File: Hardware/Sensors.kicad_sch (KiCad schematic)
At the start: 61 parts, among them J10 VL530X Connector, J11 VL530X Connector, J12 VL530X Connector, J13 VL530X Connector, J5 BNO055 Breakout, J8 VL530X Connector, J9 VL530X Connector, Q10 Q_NMOS_GSD, Q11 Q_NMOS_GSD, Q12 Q_NMOS_GSD, Q13 TEFT4300, Q2 Q_NMOS_GSD, Q3 TEFT4300, Q4 TEFT4300, Q5 TEFT4300, Q6 TEFT4300, Q7 TEFT4300, Q8 Q_NMOS_GSD, Q9 Q_NMOS_GSD

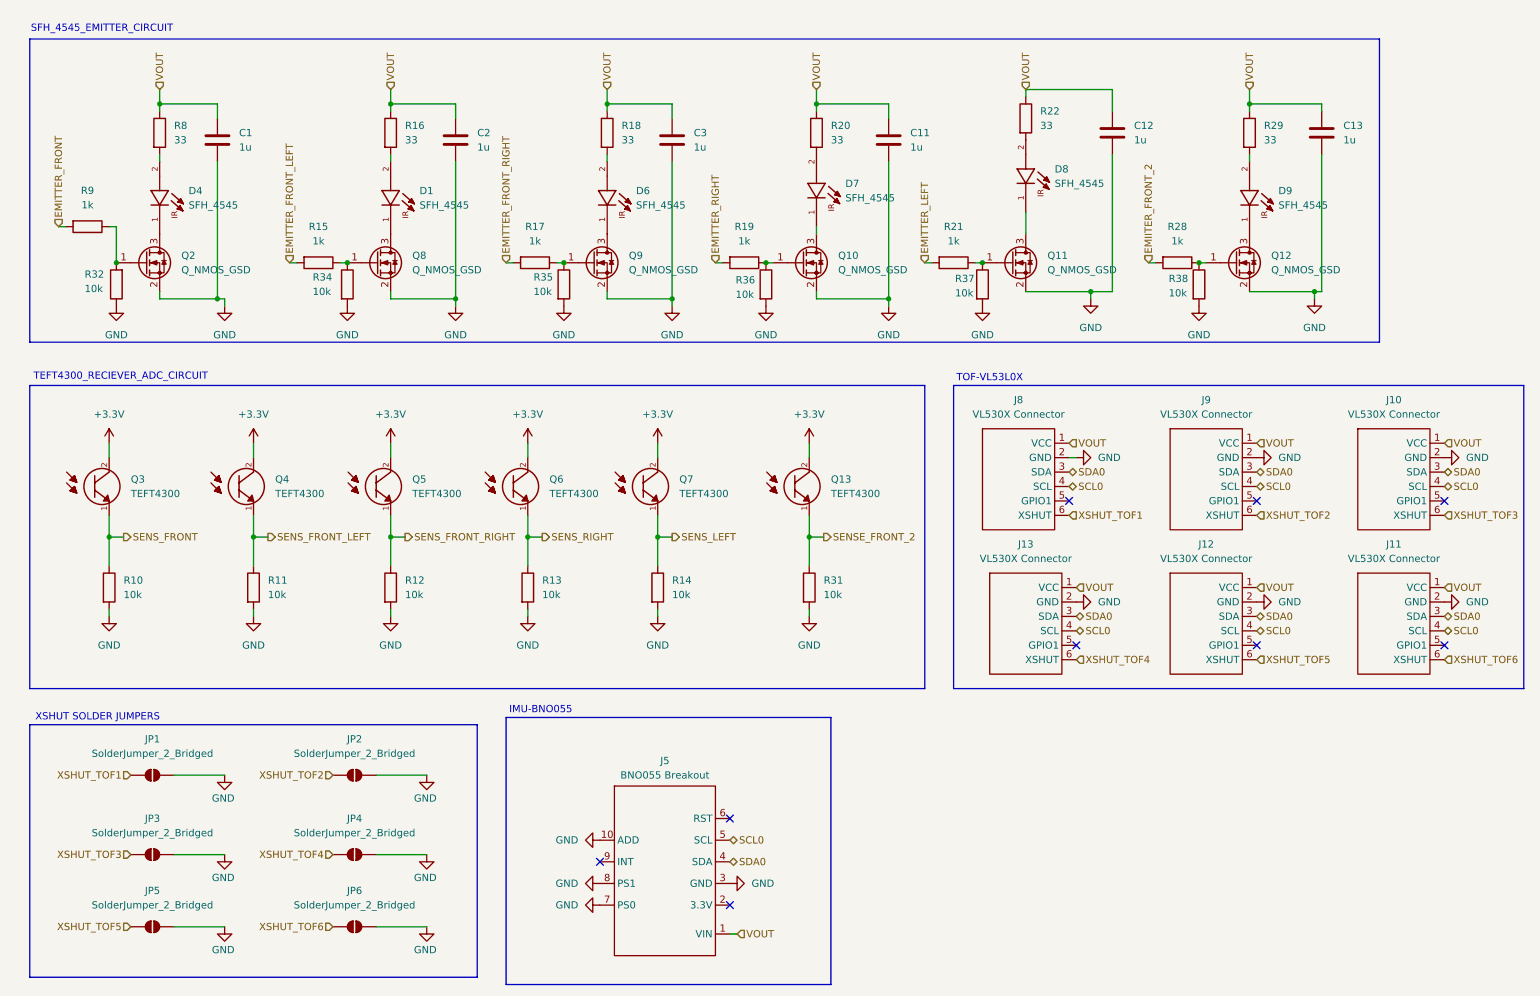
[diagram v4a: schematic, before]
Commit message: 1)PCB tracing continued, power traces need to verified,signal traces almost done except xshut, need to verify drv8833 dimesnions, should resolve teensy 4.1 error, switches footprint need to be changed. 2) changed schematic for optimum tracing in pcb editor,removed oled and added one more extra i2c bus to prevent i2c locking
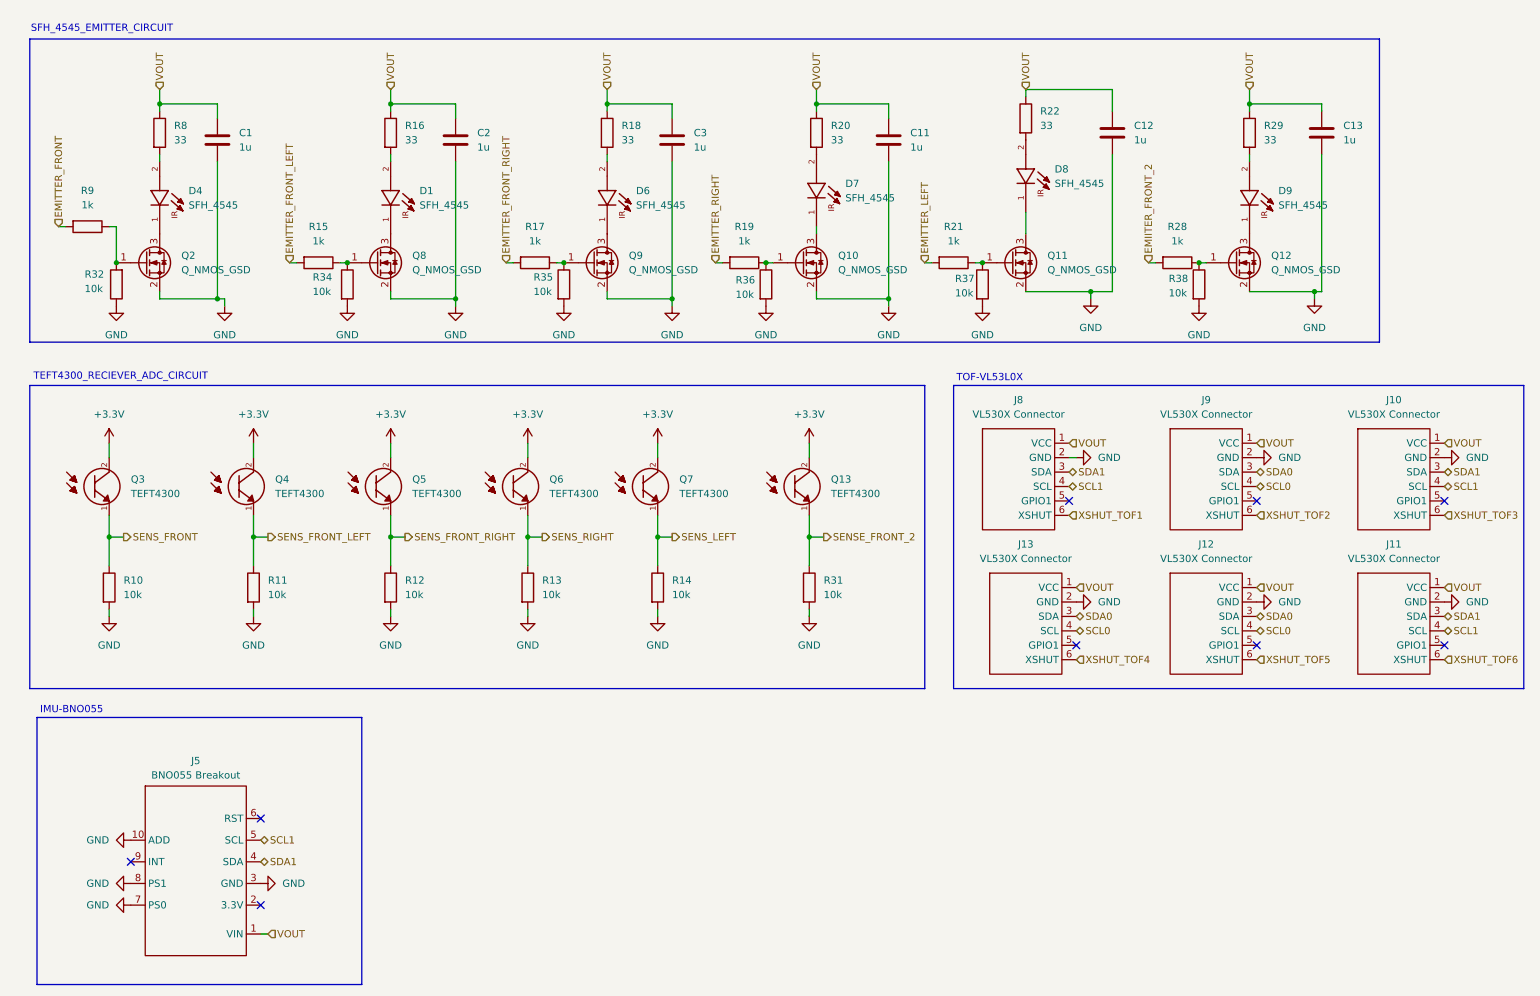
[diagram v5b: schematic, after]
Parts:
- removed JP1, JP2, JP3, JP4, JP5, JP6: SolderJumper_2_Bridged, Jumper:SolderJumper-2_P1.3mm_Open_RoundedPad1.0x1.5mm, symbol Jumper:SolderJumper_2_Open
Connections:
- net SCL0: no longer J10.4 (SCL), J11.4 (SCL), J5.5 (SCL), J8.4 (SCL)
- net SDA0: no longer J10.3 (SDA), J11.3 (SDA), J5.4 (SDA), J8.3 (SDA)
- new net SCL1: J10.4 (SCL), J11.4 (SCL), J5.5 (SCL), J8.4 (SCL)
- new net SDA1: J10.3 (SDA), J11.3 (SDA), J5.4 (SDA), J8.3 (SDA)
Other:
- note removed: "XSHUT SOLDER JUMPERS"
- moved on the sheet: J5

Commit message: Final updated pcb and schematic before dfm check
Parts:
- removed J5: BNO055 Breakout, Micromouse_Footprints:BNO055, symbol HSM_Symbols:BNO055_Breakout_Board
- added J14: BNO085 Breakout, Micromouse_Footprints:BNO085, symbol HSM_Symbols:BNO085
- added J5: Conn_01x08_Pin, Connector_PinSocket_2.54mm:PinSocket_1x08_P2.54mm_Vertical, symbol Connector:Conn_01x08_Pin
- C1, C11, C12, C13, C2, C3: footprint Capacitor_SMD:C_0603_1608Metric -> Capacitor_SMD:C_0603_1608Metric_Pad1.08x0.95mm_HandSolder
- D1, D4, D6, D7, D8, D9: footprint LED_THT:LED_D5.0mm -> SFH_4545:DIO_SFH_4545
- Q13, Q3, Q4, Q5, Q6, Q7: footprint LED_THT:LED_D3.0mm -> TEFT4300 (2):XDCR_TEFT4300
- R10, R11, R12, R13, R14, R15, R16, R17, R18, R19, R20, R21, R22, R28, R29, R31, R32, R34, R35, R36, R37, R38, R8, R9: footprint Resistor_SMD:R_0603_1608Metric -> Resistor_SMD:R_0603_1608Metric_Pad0.98x0.95mm_HandSolder
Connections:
- net +3.3V: now also J14.16 (3V3), J14.2 (3V3), J5.1 (Pin_1)
- net GND: now also J14.1 (GND), J14.12 (PS0), J14.13 (PS1), J14.15 (GND), J5.2 (Pin_2), J5.7 (Pin_7)
- net SCL1: now also J14.10 (SCL), J5.3 (Pin_3)
- net SDA1: now also J14.9 (SDA), J5.4 (Pin_4)
- net VOUT renamed +5V
- new net INT_GPIO: J14.11 (INT), J5.8 (Pin_8)
- new net RST_GPIO: J14.8 (RST)
- no-connect marks 9 -> 14
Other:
- note added: "IMU-BNO085"
- note added: "MPU6050"
- note removed: "IMU-BNO055"

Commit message: Ignore KiCad .history folder
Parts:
- J14: footprint Micromouse_Footprints:BNO085 -> Micromouse:BNO085
- R16, R18, R20, R22, R29, R8: value 33 -> 39
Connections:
- net SCL0: now also J12.3 (SCL), J13.3 (SCL), J9.3 (SCL); no longer J12.4 (SCL), J13.4 (SCL), J9.4 (SCL)
- net SCL1: now also J10.3 (SCL), J11.3 (SCL), J8.3 (SCL); no longer J10.4 (SCL), J11.4 (SCL), J8.4 (SCL)
- net SDA0: now also J12.4 (SDA), J13.4 (SDA), J9.4 (SDA); no longer J12.3 (SDA), J13.3 (SDA), J9.3 (SDA)
- net SDA1: now also J10.4 (SDA), J11.4 (SDA), J8.4 (SDA); no longer J10.3 (SDA), J11.3 (SDA), J8.3 (SDA)

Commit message: updated the dimensiosn of tb6612,shifted placements based on dfm check, other changes
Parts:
- R16, R18, R20, R22, R29, R8: value 39 -> 36.5; footprint Resistor_SMD:R_0603_1608Metric_Pad0.98x0.95mm_HandSolder -> Resistor_SMD:R_1210_3225Metric_Pad1.30x2.65mm_HandSolder
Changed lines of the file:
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@@
 			)
 		)
-		(property "Value" "39"
+		(property "Value" "36.5"
 			(at 43.18 36.8299 0)
 			(show_name no)
@@
 			)
 		)
-		(property "Footprint" "Resistor_SMD:R_0603_1608Metric_Pad0.98x0.95mm_HandSolder"
+		(property "Footprint" "Resistor_SMD:R_1210_3225Metric_Pad1.30x2.65mm_HandSolder"
 			(at 38.862 35.56 90)
 			(hide yes)
@@
 			)
 		)
-		(property "Value" "39"
+		(property "Value" "36.5"
 			(at 234.95 36.8299 0)
 			(show_name no)
@@
 			)
 		)
-		(property "Footprint" "Resistor_SMD:R_0603_1608Metric_Pad0.98x0.95mm_HandSolder"
+		(property "Footprint" "Resistor_SMD:R_1210_3225Metric_Pad1.30x2.65mm_HandSolder"
 			(at 230.632 35.56 90)
 			(hide yes)
@@
 			)
 		)
-		(property "Value" "39"
+		(property "Value" "36.5"
 			(at 195.58 34.2899 0)
 			(show_name no)
@@
 			)
 		)
-		(property "Footprint" "Resistor_SMD:R_0603_1608Metric_Pad0.98x0.95mm_HandSolder"
+		(property "Footprint" "Resistor_SMD:R_1210_3225Metric_Pad1.30x2.65mm_HandSolder"
 			(at 191.262 33.02 90)
 			(hide yes)
@@
 			)
 		)
-		(property "Value" "39"
+		(property "Value" "36.5"
 			(at 121.92 36.8299 0)
 			(show_name no)
@@
 			)
 		)
-		(property "Footprint" "Resistor_SMD:R_0603_1608Metric_Pad0.98x0.95mm_HandSolder"
+		(property "Footprint" "Resistor_SMD:R_1210_3225Metric_Pad1.30x2.65mm_HandSolder"
 			(at 117.602 35.56 90)
 			(hide yes)
@@
 			)
 		)
-		(property "Value" "39"
+		(property "Value" "36.5"
 			(at 158.75 36.8299 0)
 			(show_name no)
@@
 			)
 		)
-		(property "Footprint" "Resistor_SMD:R_0603_1608Metric_Pad0.98x0.95mm_HandSolder"
+		(property "Footprint" "Resistor_SMD:R_1210_3225Metric_Pad1.30x2.65mm_HandSolder"
 			(at 154.432 35.56 90)
 			(hide yes)
@@
 			)
 		)
-		(property "Value" "39"
+		(property "Value" "36.5"
 			(at 83.82 36.8299 0)
 			(show_name no)
@@
 			)
 		)
-		(property "Footprint" "Resistor_SMD:R_0603_1608Metric_Pad0.98x0.95mm_HandSolder"
+		(property "Footprint" "Resistor_SMD:R_1210_3225Metric_Pad1.30x2.65mm_HandSolder"
 			(at 79.502 35.56 90)
 			(hide yes)
